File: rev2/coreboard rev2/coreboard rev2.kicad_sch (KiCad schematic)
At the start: 86 parts, among them J1 RJ45_LED_Shielded, SW1 SW_Push, SW10 SW_Push, SW11 SW_Push, SW12 SW_Push, SW13 SW_Push, SW14 SW_Push, SW15 SW_Push, SW16 SW_SPDT, SW2 SW_Push, SW3 SW_Push, SW4 SW_Push, SW5 SW_Push, SW6 SW_Push, SW7 SW_Push, SW8 SW_Push, SW9 SW_Push, U1 Teensy4.1_DEV-16771, U3 SHHD003A0A, U4 74HC148, U5 74HC148, U6 74HC00, U7 OKI

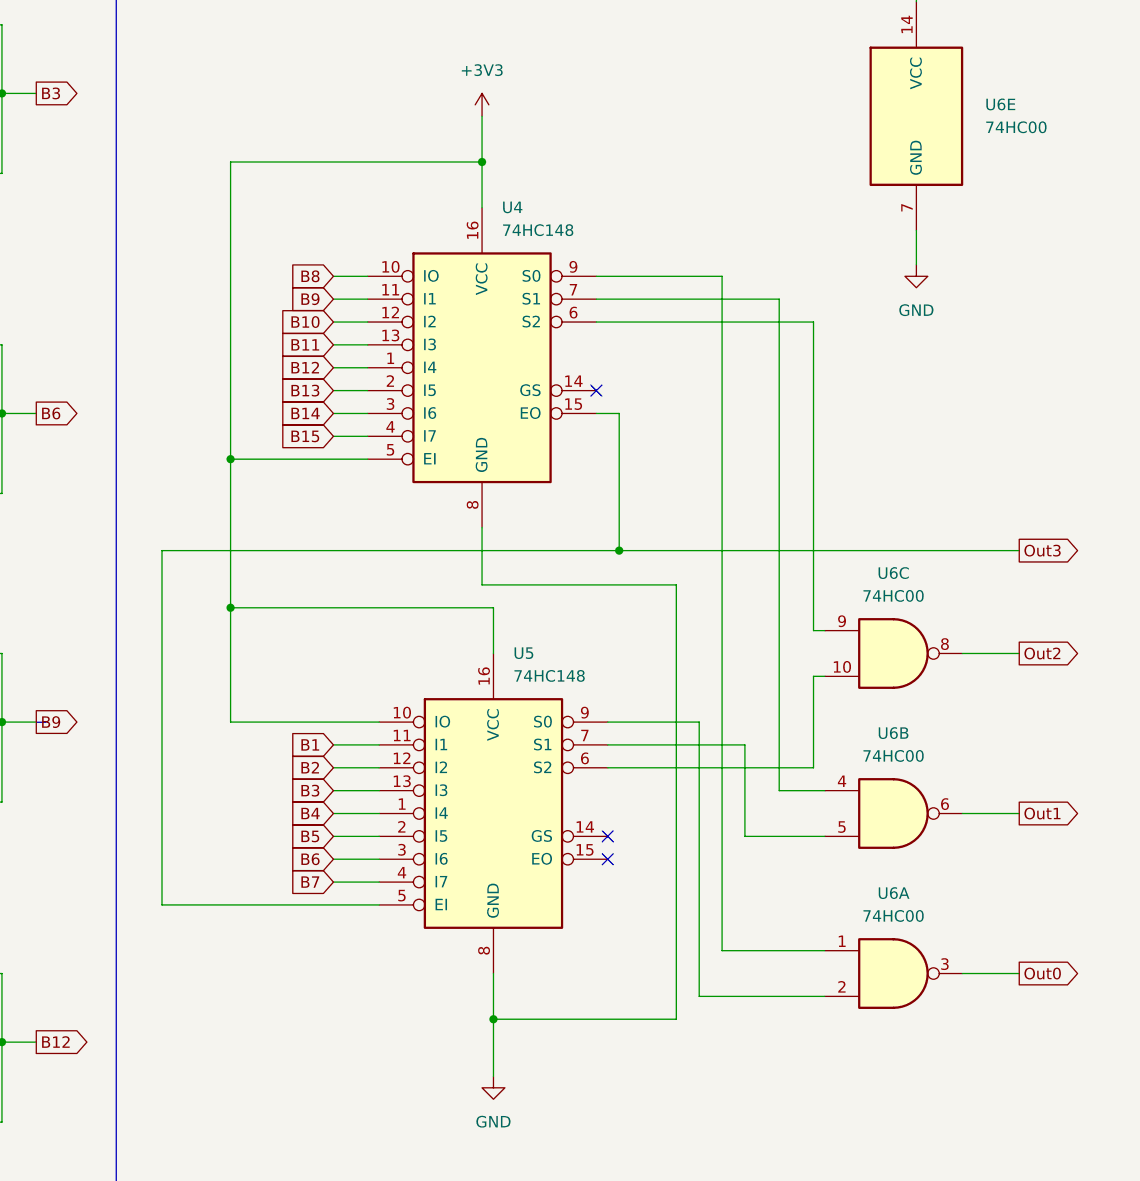
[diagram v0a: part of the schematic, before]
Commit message: put enable pins on encoders to ground
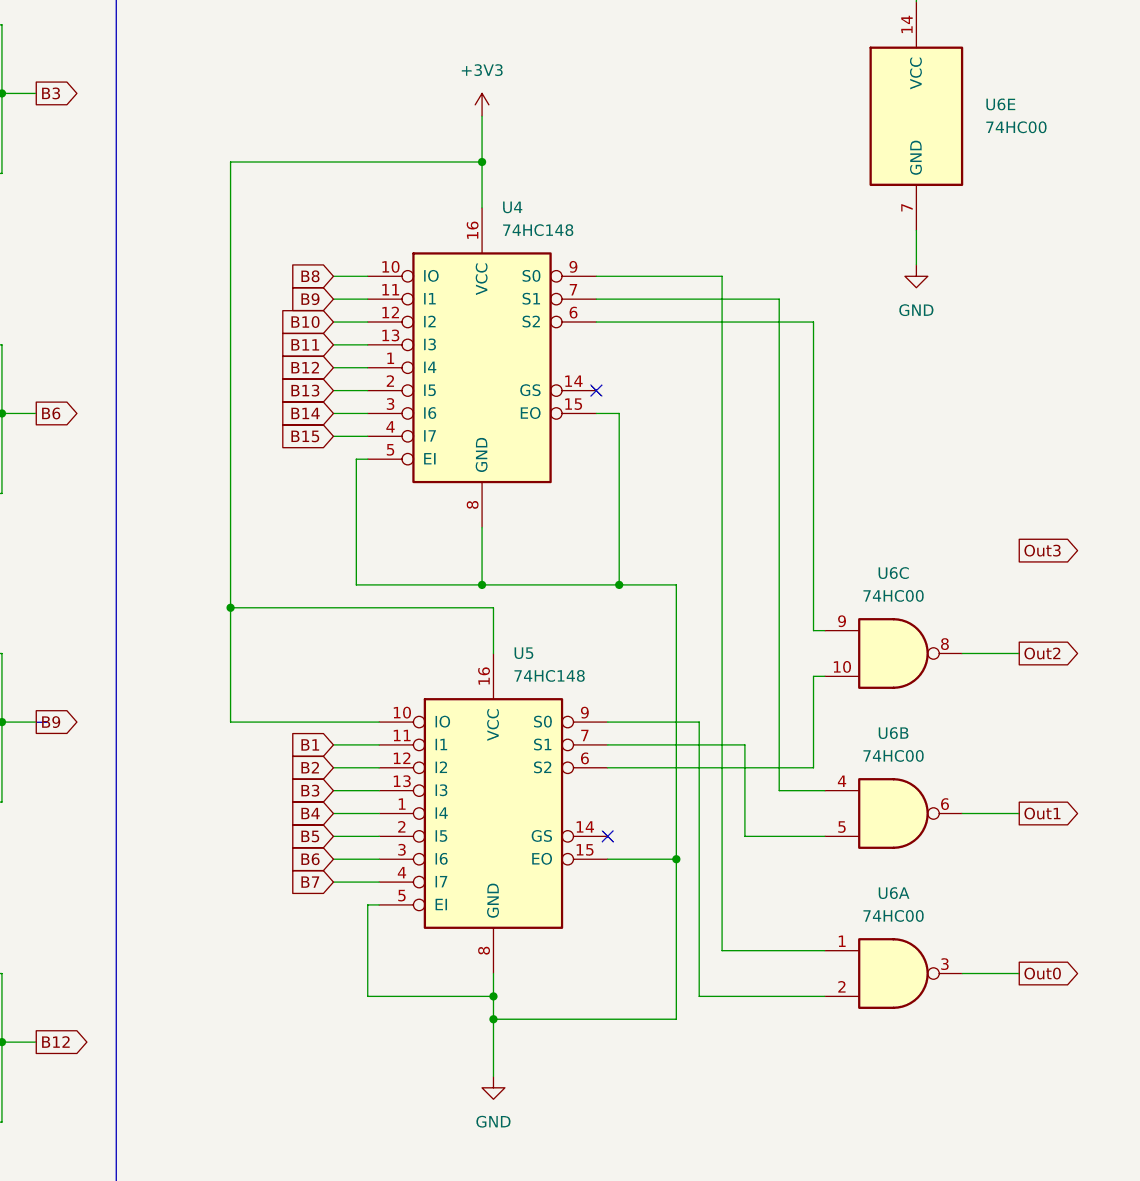
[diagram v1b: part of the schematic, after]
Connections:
- net +3V3: no longer U4.5 (EI)
- net GND: now also U4.15 (EO), U4.5 (EI), U5.15 (EO), U5.5 (EI)
- net Out3: no longer U4.15 (EO), U5.5 (EI)
- no-connect marks 29 -> 28
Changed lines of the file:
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@@
   (junction (at 48.26 40.64) (diameter 0) (color 0 0 0 0)
   )
-  (junction (at 308.61 160.02) (diameter 0) (color 0 0 0 0)
-  )
-  (junction (at 351.79 170.18) (diameter 0) (color 0 0 0 0)
-  )
   (junction (at 120.65 182.88) (diameter 0) (color 0 0 0 0)
   )
@@
   (junction (at 337.82 63.5) (diameter 0) (color 0 0 0 0)
   )
+  (junction (at 351.79 173.99) (diameter 0) (color 0 0 0 0)
+  )
   (junction (at 247.65 154.94) (diameter 0) (color 0 0 0 0)
   )
@@
   (junction (at 336.55 127) (diameter 0) (color 0 0 0 0)
   )
+  (junction (at 336.55 173.99) (diameter 0) (color 0 0 0 0)
+  )
   (junction (at 311.15 48.26) (diameter 0) (color 0 0 0 0)
   )
@@
   (junction (at 340.36 40.64) (diameter 0) (color 0 0 0 0)
   )
+  (junction (at 337.82 219.71) (diameter 0) (color 0 0 0 0)
+  )
   (junction (at 213.36 49.53) (diameter 0) (color 0 0 0 0)
   )
@@
   )
   (junction (at 213.36 41.91) (diameter 0) (color 0 0 0 0)
+  )
+  (junction (at 358.14 204.47) (diameter 0) (color 0 0 0 0)
   )
   (no_connect (at 132.08 41.91))
@@
   (no_connect (at 93.98 256.54))
   (no_connect (at 53.34 195.58))
-  (no_connect (at 350.52 204.47))
   (no_connect (at 124.46 195.58))
   (no_connect (at 93.98 200.66))
@@
     (stroke (width 0) (type default))
   )
+  (wire (pts (xy 337.82 219.71) (xy 337.82 222.25))
+    (stroke (width 0) (type default))
+  )
   (wire (pts (xy 212.09 39.37) (xy 215.9 39.37))
     (stroke (width 0) (type default))
@@
     (stroke (width 0) (type default))
   )
+  (wire (pts (xy 323.85 219.71) (xy 337.82 219.71))
+    (stroke (width 0) (type default))
+  )
   (wire (pts (xy 31.75 110.49) (xy 31.75 107.95))
     (stroke (width 0) (type default))
   )
+  (wire (pts (xy 336.55 167.64) (xy 336.55 173.99))
+    (stroke (width 0) (type default))
+  )
   (wire (pts (xy 314.96 38.1) (xy 308.61 38.1))
     (stroke (width 0) (type default))
@@
     (stroke (width 0) (type default))
   )
-  (wire (pts (xy 308.61 160.02) (xy 323.85 160.02))
-    (stroke (width 0) (type default))
-  )
   (wire (pts (xy 105.41 190.5) (xy 93.98 190.5))
     (stroke (width 0) (type default))
@@
     (stroke (width 0) (type default))
   )
+  (wire (pts (xy 322.58 160.02) (xy 322.58 173.99))
+    (stroke (width 0) (type default))
+  )
   (wire (pts (xy 260.35 181.61) (xy 261.62 181.61))
     (stroke (width 0) (type default))
@@
     (stroke (width 0) (type default))
   )
+  (wire (pts (xy 358.14 204.47) (xy 358.14 222.25))
+    (stroke (width 0) (type default))
+  )
   (wire (pts (xy 241.3 163.83) (xy 247.65 163.83))
     (stroke (width 0) (type default))
@@
     (stroke (width 0) (type default))
   )
+  (wire (pts (xy 350.52 204.47) (xy 358.14 204.47))
+    (stroke (width 0) (type default))
+  )
   (wire (pts (xy 369.57 34.29) (xy 369.57 40.64))
     (stroke (width 0) (type default))
@@
     (stroke (width 0) (type default))
   )
-  (wire (pts (xy 300.99 170.18) (xy 300.99 209.55))
-    (stroke (width 0) (type default))
-  )
   (wire (pts (xy 99.06 266.7) (xy 99.06 269.24))
     (stroke (width 0) (type default))
@@
     (stroke (width 0) (type default))
   )
-  (wire (pts (xy 351.79 170.18) (xy 396.24 170.18))
-    (stroke (width 0) (type default))
-  )
   (wire (pts (xy 240.03 259.08) (xy 247.65 259.08))
     (stroke (width 0) (type default))
@@
     (stroke (width 0) (type default))
   )
-  (wire (pts (xy 308.61 160.02) (xy 308.61 176.53))
+  (wire (pts (xy 308.61 127) (xy 308.61 176.53))
     (stroke (width 0) (type default))
   )
@@
     (stroke (width 0) (type default))
   )
-  (wire (pts (xy 358.14 173.99) (xy 358.14 222.25))
+  (wire (pts (xy 358.14 173.99) (xy 358.14 204.47))
     (stroke (width 0) (type default))
   )
@@
     (stroke (width 0) (type default))
   )
+  (wire (pts (xy 322.58 173.99) (xy 336.55 173.99))
+    (stroke (width 0) (type default))
+  )
   (polyline (pts (xy 287.02 189.23) (xy 288.29 189.23))
     (stroke (width 0) (type default))
   )
-  (wire (pts (xy 308.61 127) (xy 308.61 160.02))
-    (stroke (width 0) (type default))
-  )
   (wire (pts (xy 134.62 135.89) (xy 127 135.89))
     (stroke (width 0) (type default))
@@
     (stroke (width 0) (type default))
   )
+  (wire (pts (xy 351.79 173.99) (xy 358.14 173.99))
+    (stroke (width 0) (type default))
+  )
   (wire (pts (xy 212.09 251.46) (xy 212.09 259.08))
     (stroke (width 0) (type default))
@@
     (stroke (width 0) (type default))
   )
+  (wire (pts (xy 323.85 160.02) (xy 322.58 160.02))
+    (stroke (width 0) (type default))
+  )
   (wire (pts (xy 283.21 251.46) (xy 283.21 259.08))
     (stroke (width 0) (type default))
@@
     (stroke (width 0) (type default))
   )
+  (wire (pts (xy 351.79 154.94) (xy 351.79 173.99))
+    (stroke (width 0) (type default))
+  )
   (wire (pts (xy 212.09 163.83) (xy 212.09 154.94))
     (stroke (width 0) (type default))
@@
     (stroke (width 0) (type default))
   )
-  (wire (pts (xy 351.79 154.94) (xy 351.79 170.18))
-    (stroke (width 0) (type default))
-  )
   (wire (pts (xy 337.82 63.5) (xy 367.03 63.5))
     (stroke (width 0) (type default))
@@
     (stroke (width 0) (type default))
   )
-  (wire (pts (xy 336.55 173.99) (xy 358.14 173.99))
+  (wire (pts (xy 336.55 173.99) (xy 351.79 173.99))
     (stroke (width 0) (type default))
   )
@@
     (stroke (width 0) (type default))
   )
-  (wire (pts (xy 337.82 217.17) (xy 337.82 222.25))
+  (wire (pts (xy 337.82 217.17) (xy 337.82 219.71))
     (stroke (width 0) (type default))
   )
@@
     (stroke (width 0) (type default))
   )
+  (wire (pts (xy 323.85 209.55) (xy 323.85 219.71))
+    (stroke (width 0) (type default))
+  )
   (wire (pts (xy 369.57 40.64) (xy 373.38 40.64))
     (stroke (width 0) (type default))
@@
     (stroke (width 0) (type default))
   )
-  (wire (pts (xy 300.99 170.18) (xy 351.79 170.18))
-    (stroke (width 0) (type default))
-  )
   (wire (pts (xy 49.53 259.08) (xy 53.34 259.08))
     (stroke (width 0) (type default))
@@
     (stroke (width 0) (type default))
   )
-  (wire (pts (xy 336.55 167.64) (xy 336.55 173.99))
-    (stroke (width 0) (type default))
-  )
   (wire (pts (xy 306.07 58.42) (xy 314.96 58.42))
     (stroke (width 0) (type default))
@@
     (stroke (width 0) (type default))
   )
-  (wire (pts (xy 300.99 209.55) (xy 325.12 209.55))
-    (stroke (width 0) (type default))
-  )
   (wire (pts (xy 246.38 147.32) (xy 247.65 147.32))
     (stroke (width 0) (type default))
@@
     (stroke (width 0) (type default))
   )
+  (wire (pts (xy 325.12 209.55) (xy 323.85 209.55))
+    (stroke (width 0) (type default))
+  )
